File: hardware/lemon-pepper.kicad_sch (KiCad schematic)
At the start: 32 parts, among them J101 INPUT, M101 MOT

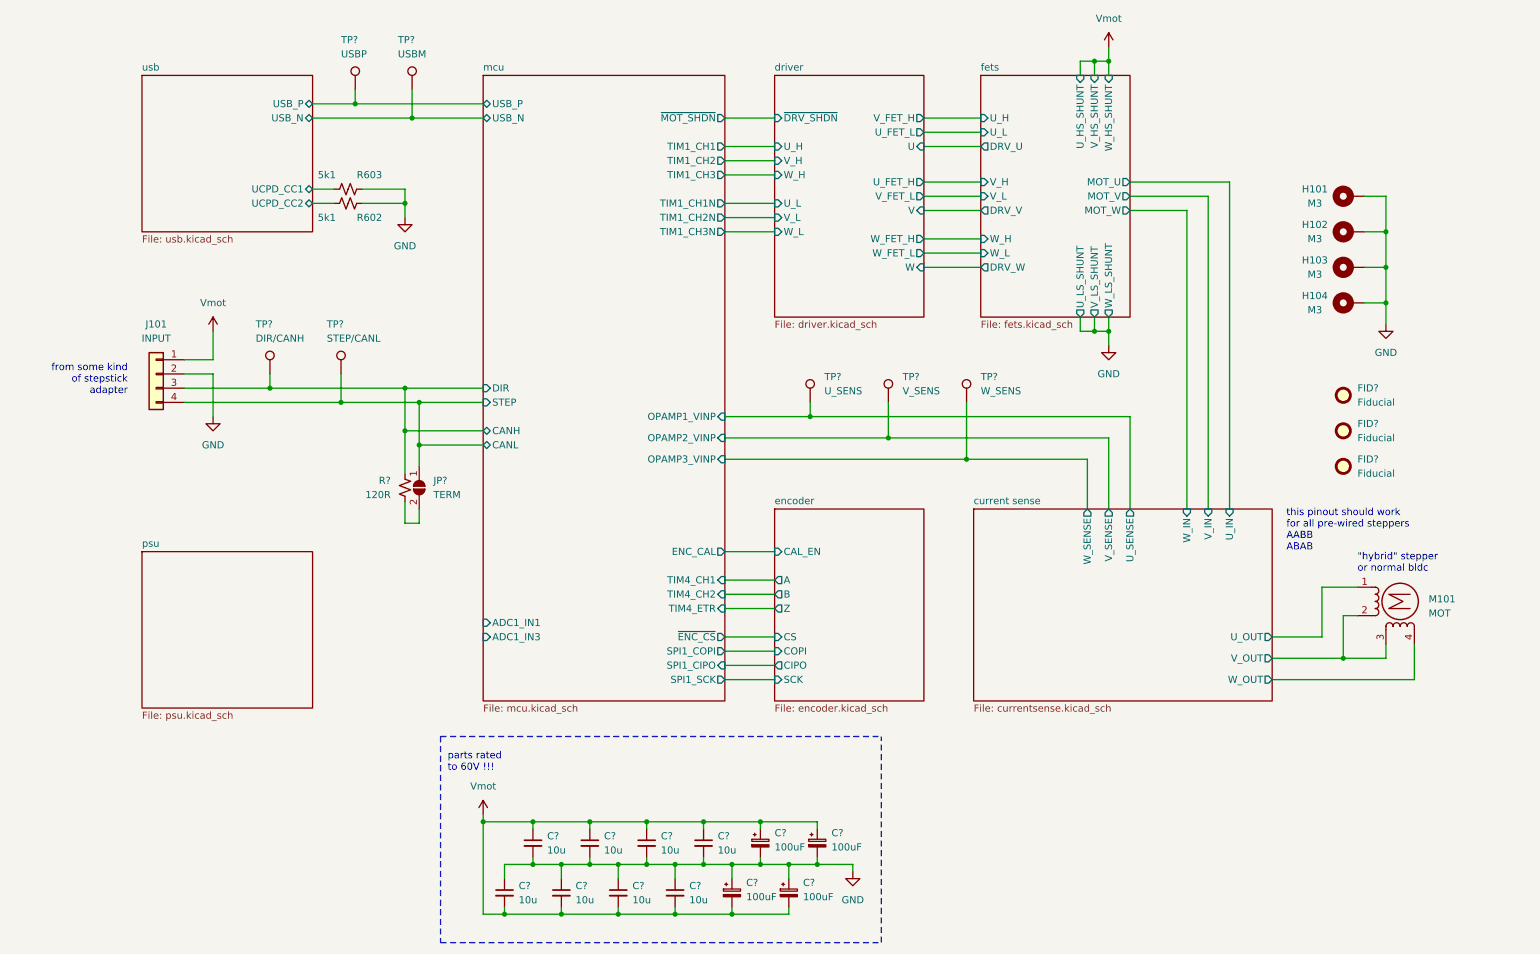
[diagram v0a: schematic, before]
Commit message: finish component selection
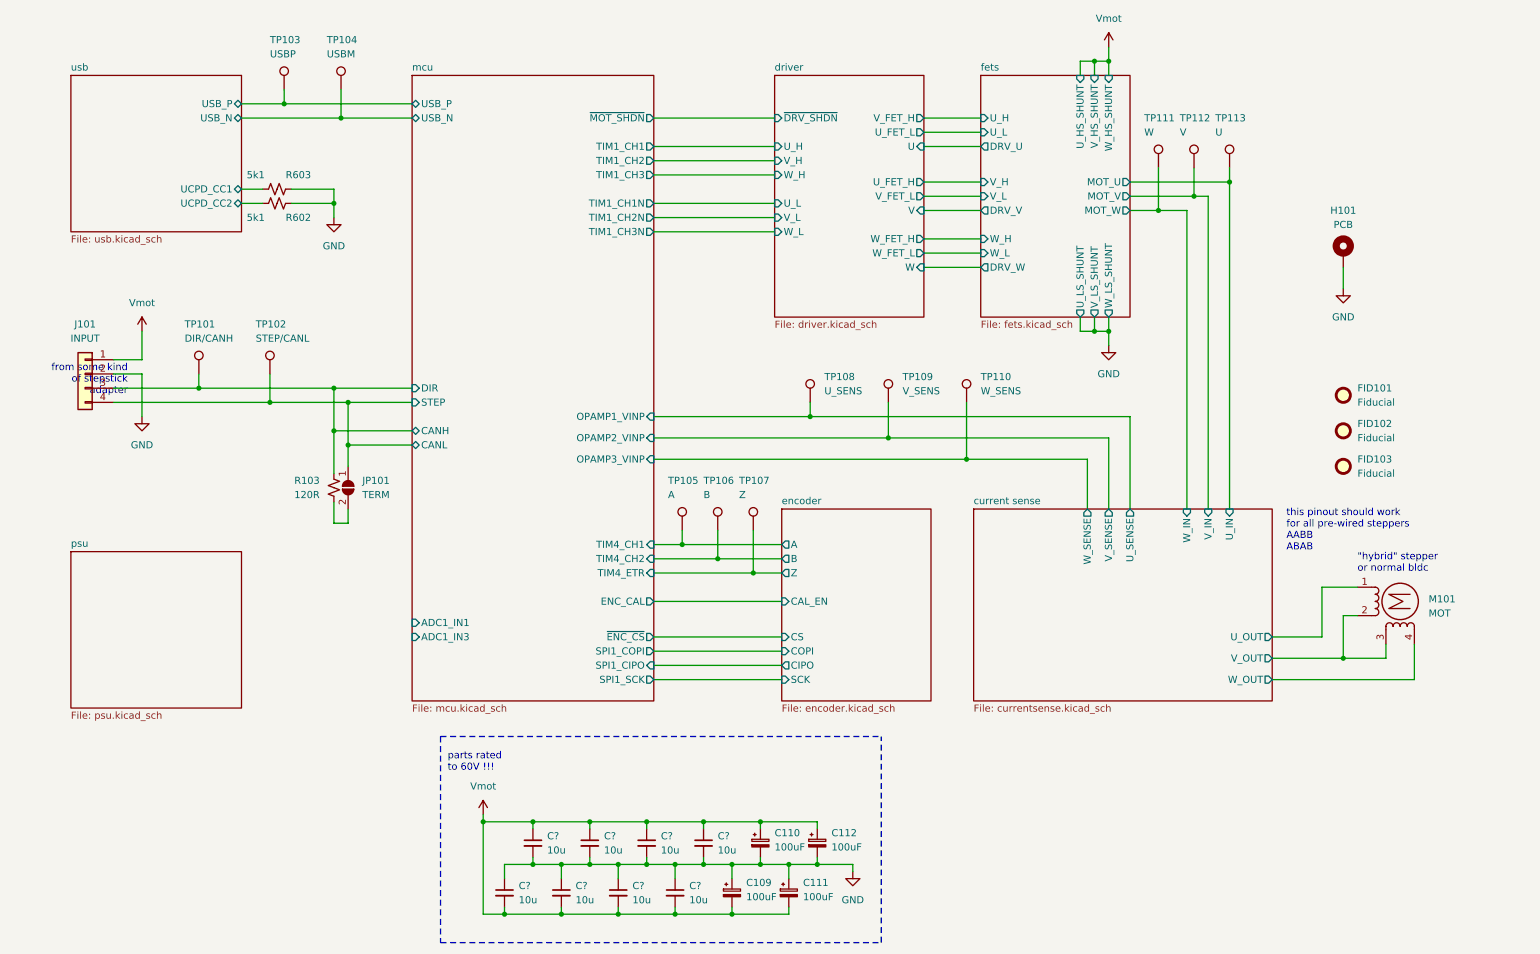
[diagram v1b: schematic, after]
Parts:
- removed H102, H103, H104: M3, MountingHole:MountingHole_3.2mm_M3_DIN965_Pad, symbol Mechanical:MountingHole_Pad
- added TP105: A, TestPoint:TestPoint_Pad_D1.0mm, symbol Connector:TestPoint
- added TP106: B, TestPoint:TestPoint_Pad_D1.0mm, symbol Connector:TestPoint
- added TP107: Z, TestPoint:TestPoint_Pad_D1.0mm, symbol Connector:TestPoint
- added TP111: W, TestPoint:TestPoint_Pad_D1.0mm, symbol Connector:TestPoint
- added TP112: V, TestPoint:TestPoint_Pad_D1.0mm, symbol Connector:TestPoint
- added TP113: U, TestPoint:TestPoint_Pad_D1.0mm, symbol Connector:TestPoint
- FID101, FID102, FID103: renamed from FID?; now left out of the parts list
- H101: value M3 -> PCB; footprint MountingHole:MountingHole_3.2mm_M3_DIN965_Pad -> mechanical:NEMA17; now left out of the parts list
- J101, M101: footprint Connector_JST:JST_XH_S4B-XH-A_1x04_P2.50mm_Horizontal -> easyeda2kicad:CONN-TH_4P-P0.20_XUNPU_WAFER-XH2.54-4PWB; LCSC Part (none) -> C3029478
- JP101: renamed from JP?; now left out of the parts list
- gave numbers to parts that had none: 12
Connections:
- net current sense/U_IN: now also TP113.1
- net current sense/V_IN: now also TP112.1
- net current sense/W_IN: now also TP111.1
- net encoder/A: now also TP105.1
- net encoder/B: now also TP106.1
- net encoder/Z: now also TP107.1
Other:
- company: (none) -> matei repair lab
- title: (none) -> LEMON PEPPER STEPPER
- moved on the sheet: H101, J101, JP101, R103, R602, R603, TP101, TP102, TP103, TP104

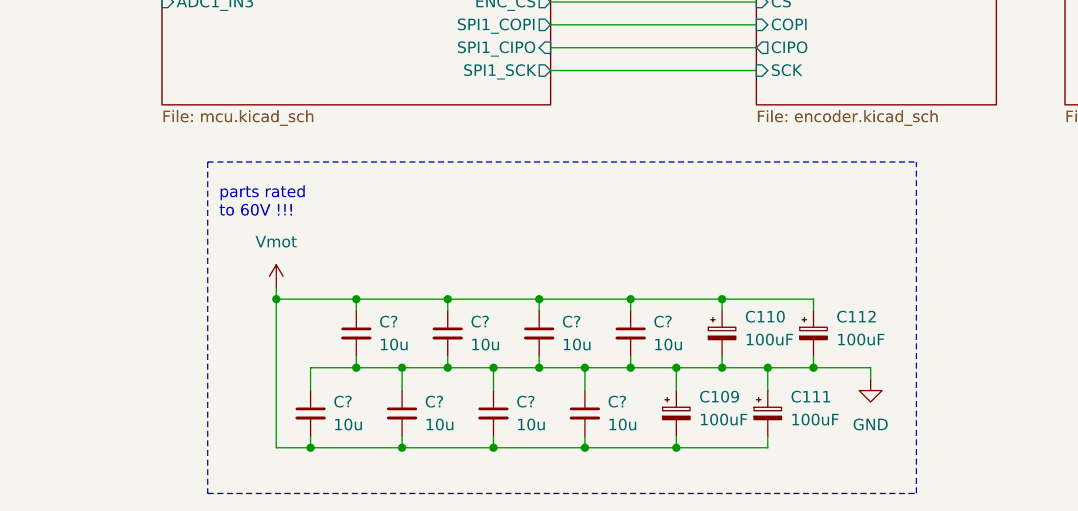
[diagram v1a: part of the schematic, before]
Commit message: reverse polarity diode
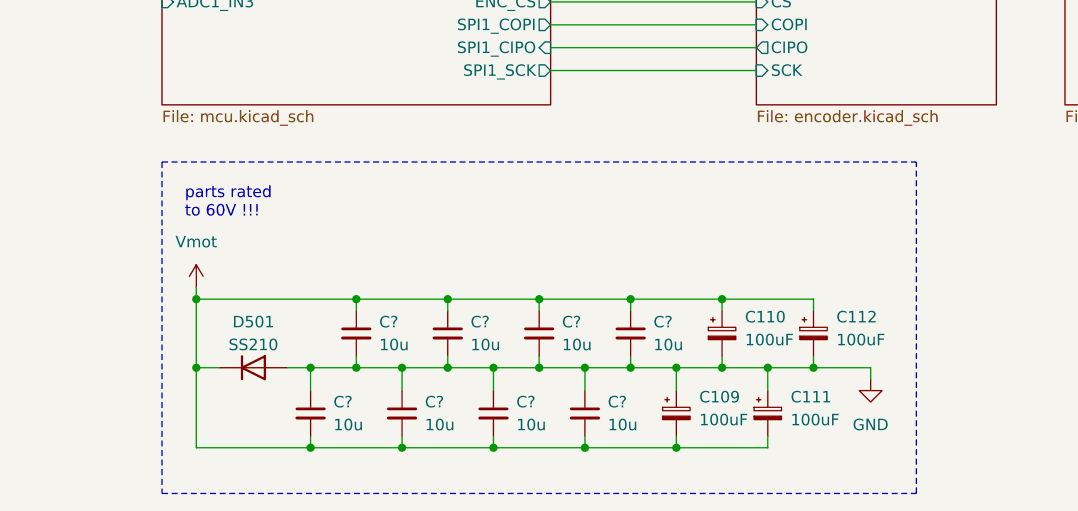
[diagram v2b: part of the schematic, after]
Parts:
- added D501: SS210, Diode_SMD:D_SMA, symbol Device:D
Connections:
- net GND: now also D501.2 (A)
- net Vmot: now also D501.1 (K)
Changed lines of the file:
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@@
   (junction (at 139.7 170.18) (diameter 0) (color 0 0 0 0)
   )
+  (junction (at 104.14 177.8) (diameter 0) (color 0 0 0 0)
+  )
   (junction (at 149.86 170.18) (diameter 0) (color 0 0 0 0)
   )
@@
   (junction (at 158.75 97.79) (diameter 0) (color 0 0 0 0)
   )
-  (junction (at 100.33 170.18) (diameter 0) (color 0 0 0 0)
+  (junction (at 91.44 170.18) (diameter 0) (color 0 0 0 0)
   )
   (junction (at 134.62 186.69) (diameter 0) (color 0 0 0 0)
@@
   (junction (at 114.3 177.8) (diameter 0) (color 0 0 0 0)
   )
+  (junction (at 91.44 177.8) (diameter 0) (color 0 0 0 0)
+  )
   (junction (at 74.93 44.45) (diameter 0) (color 0 0 0 0)
   )
@@
     (stroke (width 0) (type default))
   )
-  (polyline (pts (xy 92.71 191.77) (xy 171.45 191.77))
+  (polyline (pts (xy 87.63 191.77) (xy 171.45 191.77))
     (stroke (width 0) (type dash))
   )
@@
     (stroke (width 0) (type default))
   )
-  (wire (pts (xy 100.33 186.69) (xy 100.33 170.18))
+  (wire (pts (xy 91.44 186.69) (xy 91.44 177.8))
     (stroke (width 0) (type default))
   )
@@
     (stroke (width 0) (type default))
   )
-  (polyline (pts (xy 92.71 154.94) (xy 92.71 191.77))
+  (polyline (pts (xy 87.63 154.94) (xy 87.63 191.77))
     (stroke (width 0) (type dash))
   )
@@
     (stroke (width 0) (type default))
   )
+  (wire (pts (xy 101.6 177.8) (xy 104.14 177.8))
+    (stroke (width 0) (type default))
+  )
   (wire (pts (xy 158.75 97.79) (xy 130.81 97.79))
     (stroke (width 0) (type default))
@@
     (stroke (width 0) (type default))
   )
-  (polyline (pts (xy 92.71 154.94) (xy 171.45 154.94))
+  (polyline (pts (xy 87.63 154.94) (xy 171.45 154.94))
     (stroke (width 0) (type dash))
   )
@@
   )
   (wire (pts (xy 256.54 133.35) (xy 254 133.35))
+    (stroke (width 0) (type default))
+  )
+  (wire (pts (xy 91.44 177.8) (xy 93.98 177.8))
     (stroke (width 0) (type default))
   )
@@
     (stroke (width 0) (type dash))
   )
-  (wire (pts (xy 100.33 168.91) (xy 100.33 170.18))
+  (wire (pts (xy 91.44 168.91) (xy 91.44 170.18))
     (stroke (width 0) (type default))
   )
@@
     (stroke (width 0) (type default))
   )
+  (wire (pts (xy 91.44 177.8) (xy 91.44 170.18))
+    (stroke (width 0) (type default))
+  )
   (wire (pts (xy 158.75 95.25) (xy 158.75 97.79))
     (stroke (width 0) (type default))
@@
     (stroke (width 0) (type default))
   )
-  (wire (pts (xy 100.33 170.18) (xy 109.22 170.18))
+  (wire (pts (xy 91.44 170.18) (xy 109.22 170.18))
     (stroke (width 0) (type default))
   )
@@
     (stroke (width 0) (type default))
   )
-  (wire (pts (xy 104.14 186.69) (xy 100.33 186.69))
+  (wire (pts (xy 104.14 186.69) (xy 91.44 186.69))
     (stroke (width 0) (type default))
   )
@@
     (effects (font (size 1.27 1.27)) (justify left bottom))
   )
-  (text "parts rated\nto 60V !!!" (at 93.98 161.29 0)
+  (text "parts rated\nto 60V !!!" (at 90.17 161.29 0)
     (effects (font (size 1.27 1.27)) (justify left bottom))
   )
@@
     )
   )
-  (symbol (lib_id "matei:Vmot") (at 100.33 168.91 0) (unit 1)
+  (symbol (lib_id "matei:Vmot") (at 91.44 168.91 0) (unit 1)
     (in_bom yes) (on_board yes) (dnp no) (fields_autoplaced)
-    (property "Reference" "#PWR0713" (at 95.25 172.72 0)
-      (effects (font (size 1.27 1.27)) hide)
-    )
-    (property "Value" "Vmot" (at 100.33 163.83 0)
+    (property "Reference" "#PWR0713" (at 86.36 172.72 0)
+      (effects (font (size 1.27 1.27)) hide)
+    )
+    (property "Value" "Vmot" (at 91.44 163.83 0)
       (effects (font (size 1.27 1.27)))
     )
-    (property "Footprint" "" (at 100.33 168.91 0)
-      (effects (font (size 1.27 1.27)) hide)
-    )
-    (property "Datasheet" "" (at 100.33 168.91 0)
+    (property "Footprint" "" (at 91.44 168.91 0)
+      (effects (font (size 1.27 1.27)) hide)
+    )
+    (property "Datasheet" "" (at 91.44 168.91 0)
       (effects (font (size 1.27 1.27)) hide)
     )
@@
         )
       )
+    )
+  )
+  (symbol (lib_id "Device:D") (at 97.79 177.8 0) (unit 1)
+    (in_bom yes) (on_board yes) (dnp no)
+    (property "Reference" "D501" (at 97.79 172.72 0)
+      (effects (font (size 1.27 1.27)))
+    )
+    (property "Value" "SS210" (at 97.79 175.26 0)
+      (effects (font (size 1.27 1.27)))
+    )
+    (property "Footprint" "Diode_SMD:D_SMA" (at 97.79 177.8 0)
+      (effects (font (size 1.27 1.27)) hide)
+    )
+    (property "Datasheet" "~" (at 97.79 177.8 0)
+      (effects (font (size 1.27 1.27)) hide)
+    )
+    (property "Sim.Device" "D" (at 97.79 177.8 0)
+      (effects (font (size 1.27 1.27)) hide)
+    )
+    (property "Sim.Pins" "1=K 2=A" (at 97.79 177.8 0)
+      (effects (font (size 1.27 1.27)) hide)
+    )
+    (property "LCSC Part" "C14996" (at 97.79 177.8 0)
+      (effects (font (size 1.27 1.27)) hide)
+    )
+    (pin "1")
+    (pin "2")
+    (instances
+      (project "lemon-pepper"
+        (path "/0306e2fa-4433-4288-91d9-65a3484207ad/40d0f733-2cb2-4037-bc30-ae30111fe2e1"
+          (reference "D501") (unit 1)
+        )
+        (path "/0306e2fa-4433-4288-91d9-65a3484207ad"
+          (reference "D?") (unit 1)
+        )
+      )

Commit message: try new driver
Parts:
- H101: footprint mechanical:NEMA17 -> mechanical:NEMA14
- J101: footprint easyeda2kicad:CONN-TH_4P-P0.20_XUNPU_WAFER-XH2.54-4PWB -> Connector_JST:JST_XH_B4B-XH-A_1x04_P2.50mm_Vertical; LCSC Part C3029478 -> (none)
- M101: footprint easyeda2kicad:CONN-TH_4P-P0.20_XUNPU_WAFER-XH2.54-4PWB -> footprints:XH2.54 4P; LCSC Part C3029478 -> (none)
- gave numbers to parts that had none: 8
- renumbered D501 to D101, TP108 to TP105, TP105 to TP106, TP106 to TP107, TP109 to TP108, TP107 to TP109
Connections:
- net current sense/V_OUT: now also M101.4; no longer M101.2 (-), M101.3
- net current sense/W_OUT: now also M101.2 (-), M101.3; no longer M101.4
- net mcu/CANH: now also J101.4 (Pin_4), JP101.1 (A), TP102.1; no longer J101.3 (Pin_3), R103.1, TP101.1
- net mcu/CANL: now also J101.3 (Pin_3), R103.1, TP101.1; no longer J101.4 (Pin_4), JP101.1 (A), TP102.1
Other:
- removed sheet driver
- removed sheet fets
- added sheet half bridges (halfbridges.kicad_sch)
- sheet mcu ports: added none; removed TIM1_CH1N, TIM1_CH2N, TIM1_CH3N
- moved on the sheet: FID101, FID102, FID103, H101, J101, JP101, M101, R103, R602, R603, TP101, TP102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

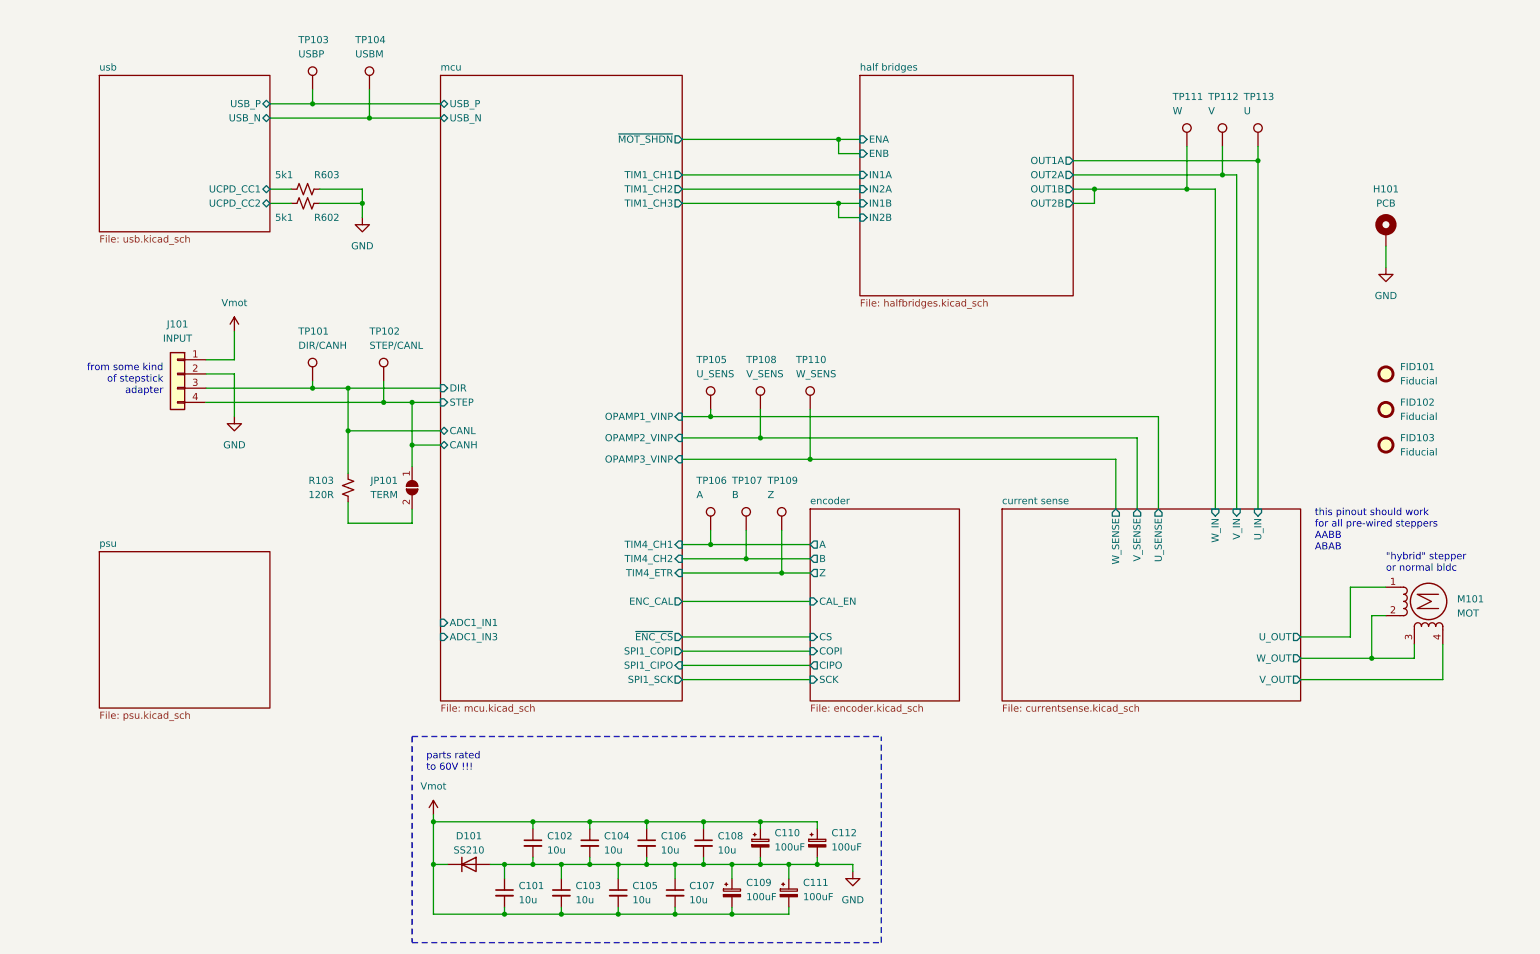
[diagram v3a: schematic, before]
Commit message: change driver configuration
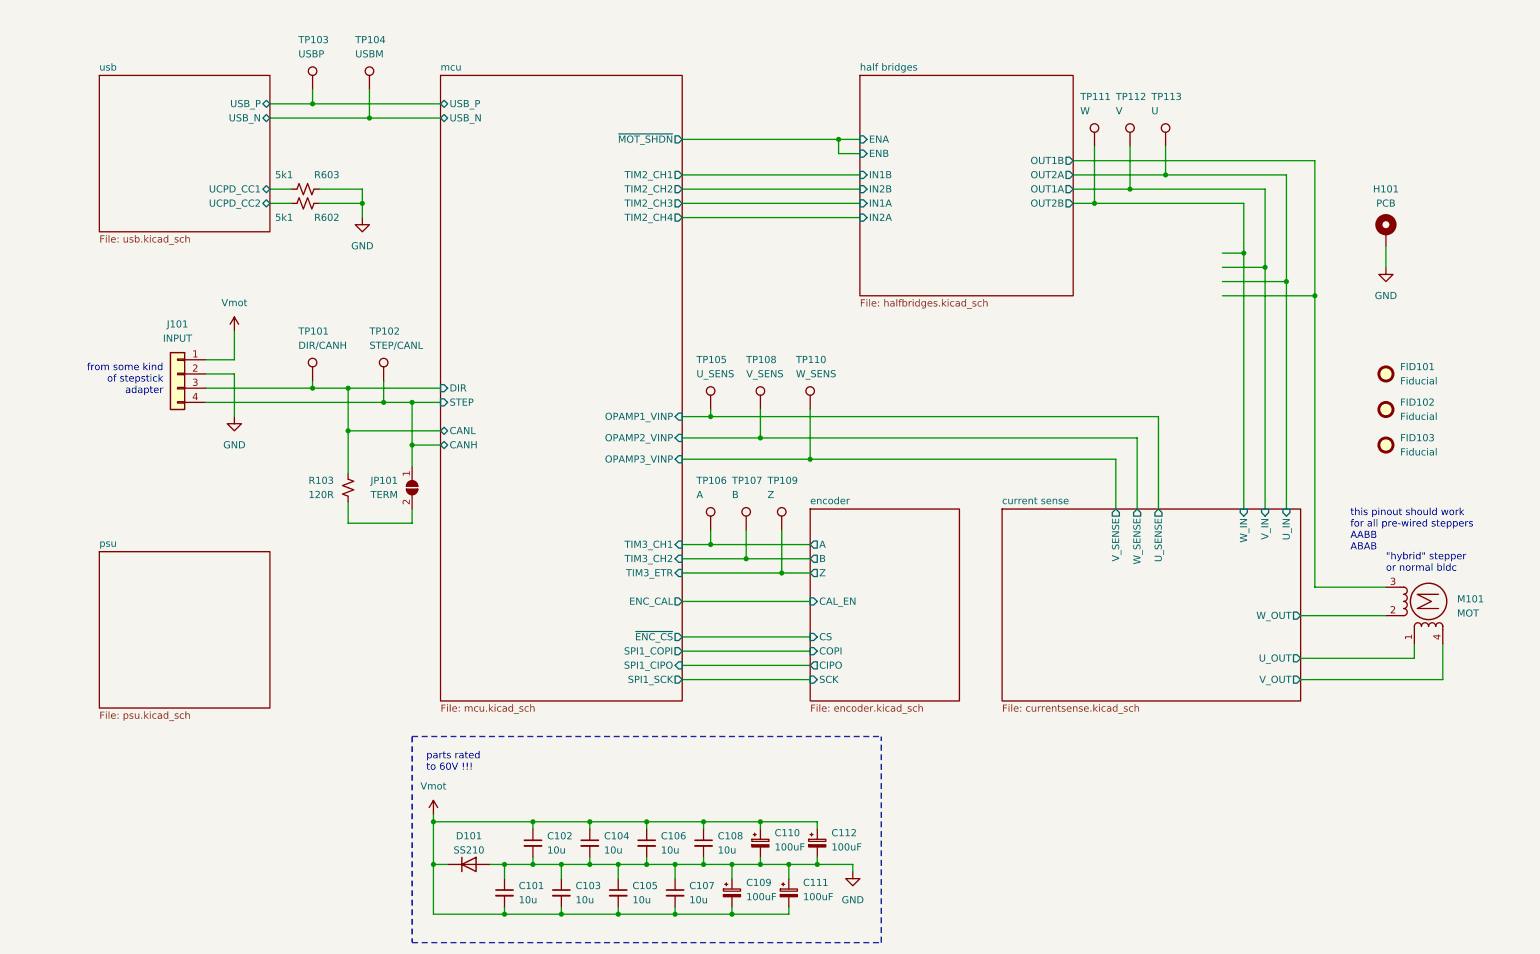
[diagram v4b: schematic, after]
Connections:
- net current sense/V_SENSE: now also TP110.1; no longer TP108.1
- net current sense/W_OUT: no longer M101.3
- net current sense/W_SENSE: now also TP108.1; no longer TP110.1
- new net half bridges/OUT1B: M101.3
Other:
- sheet mcu ports: added TIM2_CH1, TIM2_CH2, TIM2_CH3, TIM2_CH4, TIM3_CH1, TIM3_CH2, TIM3_ETR; removed ADC1_IN1, ADC1_IN3, TIM1_CH1, TIM1_CH2, TIM1_CH3, TIM4_CH1, TIM4_CH2, TIM4_ETR
- moved on the sheet: TP111, TP112, TP113
